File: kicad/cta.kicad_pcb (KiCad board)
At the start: 2 copper layers, 50.8 x 50.8 mm, 25 parts, among them Q1 2N3904, Q2 2N3906, U1 LM324

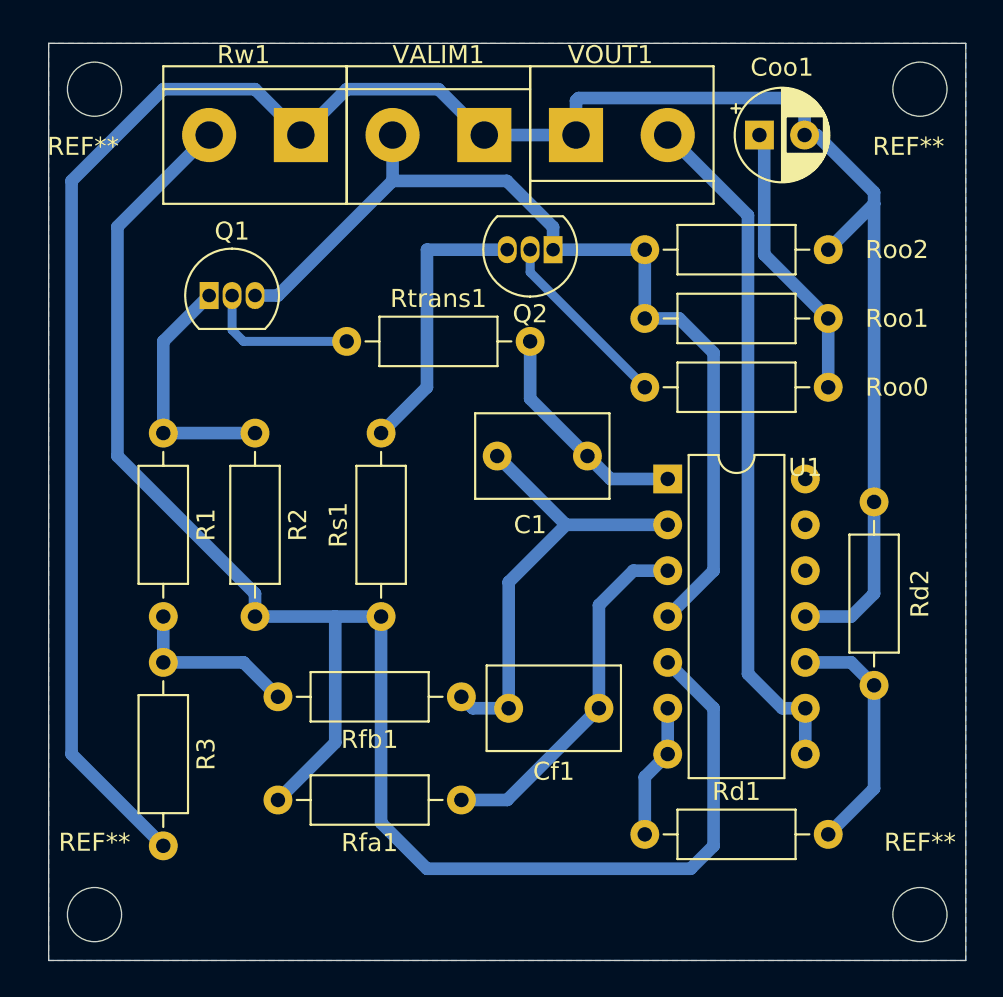
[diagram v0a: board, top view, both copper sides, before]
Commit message: Modified the warmup subcircuit
To initialize the circuit, a subcircuit was used that on powerup would
temporarily add voltage to the + leg of the op amp. Now this circuit adds
this voltage directly to the base of Q1. With this I could also remove
the resistor conecting both cricuits (Rs1).

I also decreased the fill zones tolerances and most of the board is now
filled.
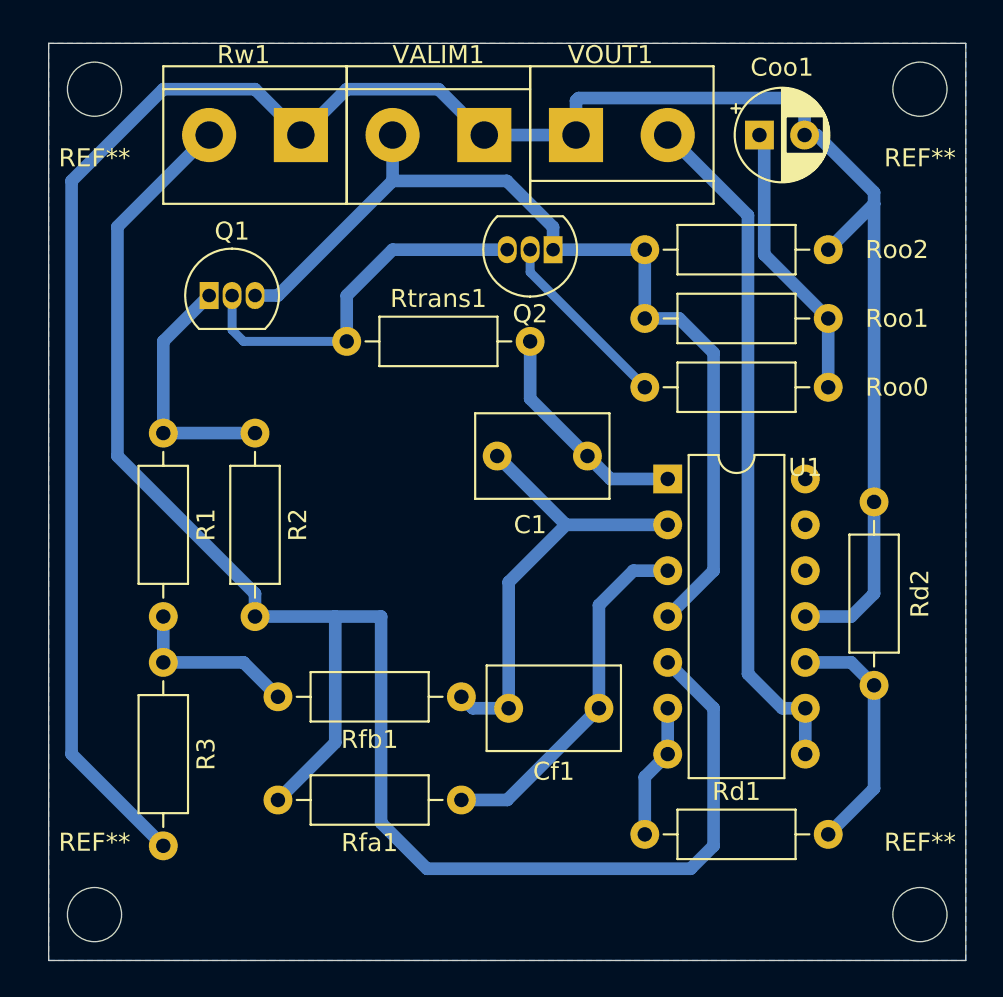
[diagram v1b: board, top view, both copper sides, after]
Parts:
- removed Rs1: 220k, Resistor_THT:R_Axial_DIN0207_L6.3mm_D2.5mm_P10.16mm_Horizontal
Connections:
- Q2 pad 3: Net-(Q2-Pad3) -> Net-(Q1-Pad2)
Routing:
- net Net-(Q2-Pad3): track 15.7 -> 0.00 mm
- net Net-(Q1-Pad2): track 8.52 -> 21.0 mm
